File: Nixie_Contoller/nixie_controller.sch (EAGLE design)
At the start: 46 parts, among them IC1 DS1307, IC2 MAX1771ESA, IC4 MPM3630GQV-P, J1 CON-SOCJ-2155, Q1 16MHz, T1 IRF644PBF, U1 328P, U2 HU2032-LF, Y2 32.768kHz

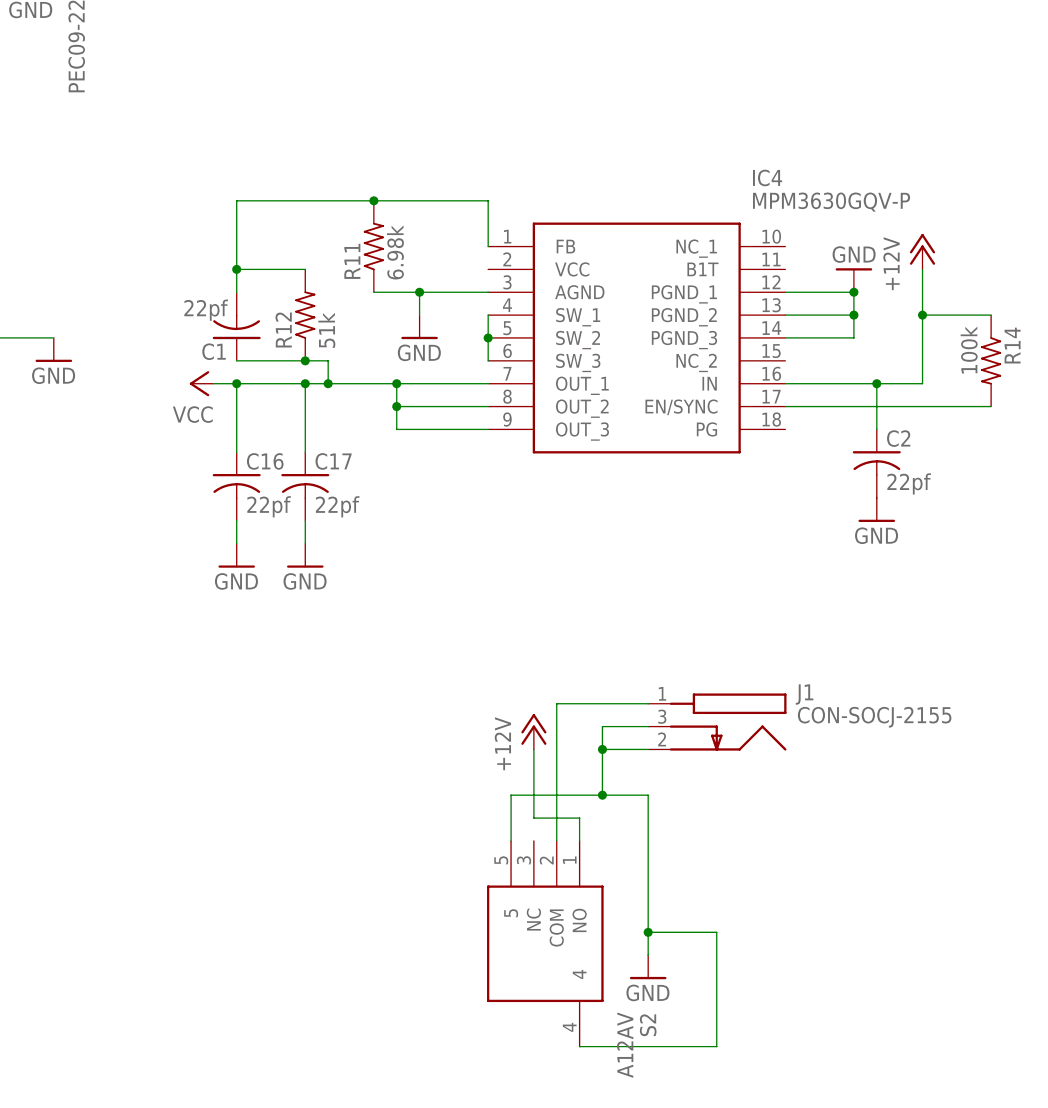
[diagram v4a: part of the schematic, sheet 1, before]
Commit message: Revert "Adds LV switching PSU"
This reverts commit 12f529c285d7cae732b9ac692bbbf0adcfd9615d.
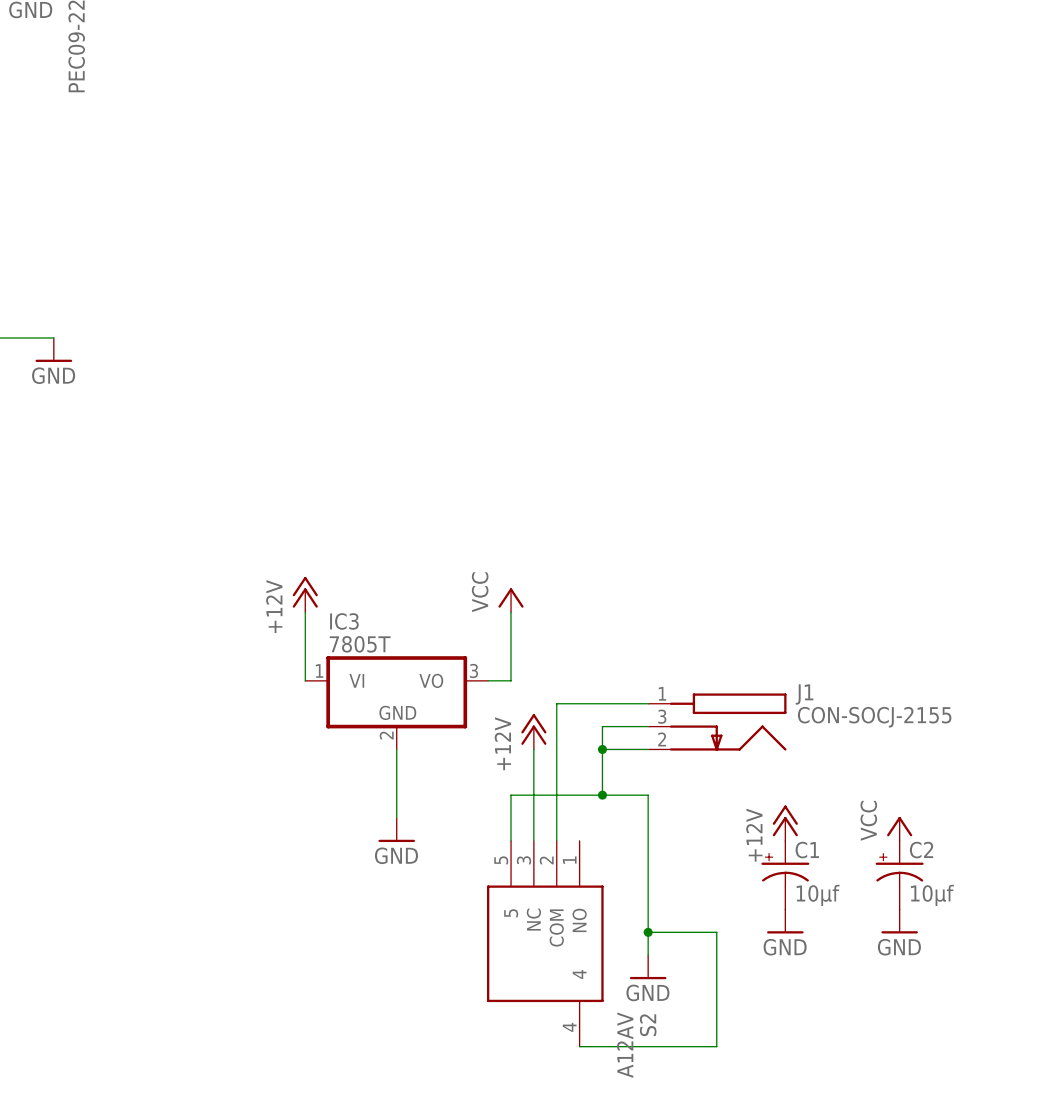
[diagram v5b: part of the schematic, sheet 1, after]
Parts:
- removed C16, C17: 22pf, rcl:C-USC0402
- removed IC4: MPM3630GQV-P, SamacSys_Parts:MPM3630GQV-P
- removed R11: 6.98k, rcl:R-US_R0201
- removed R12: 51k, rcl:R-US_R0201
- removed R14: 100k, rcl:R-US_R0201
- added IC3: 7805T, linear:7805T
- C1: value 22pf -> 10μf; device rcl:C-USC0201 -> rcl:CPOL-USE2-5
- C2: value 22pf -> 10μf; device rcl:C-USC0603 -> rcl:CPOL-USE2-5
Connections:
- removed net N$25: IC4.SW_1, IC4.SW_2, IC4.SW_3
- removed net N$28: IC4.EN/SYNC, R14.2
- removed net N$31: C1.2, IC4.FB, R11.2, R12.2
- net +12V: now also C1.+, IC3.VI, S2.NC; no longer C2.1, IC4.IN, R14.1, S2.NO
- net GND: now also C1.-, C2.-, IC3.GND; no longer C16.2, C17.2, C2.2, IC4.AGND, IC4.PGND_1, IC4.PGND_2, IC4.PGND_3, R11.1
- net VCC: now also C2.+, IC3.VO; no longer C1.1, C16.1, C17.1, IC4.OUT_1, IC4.OUT_2, IC4.OUT_3, R12.1

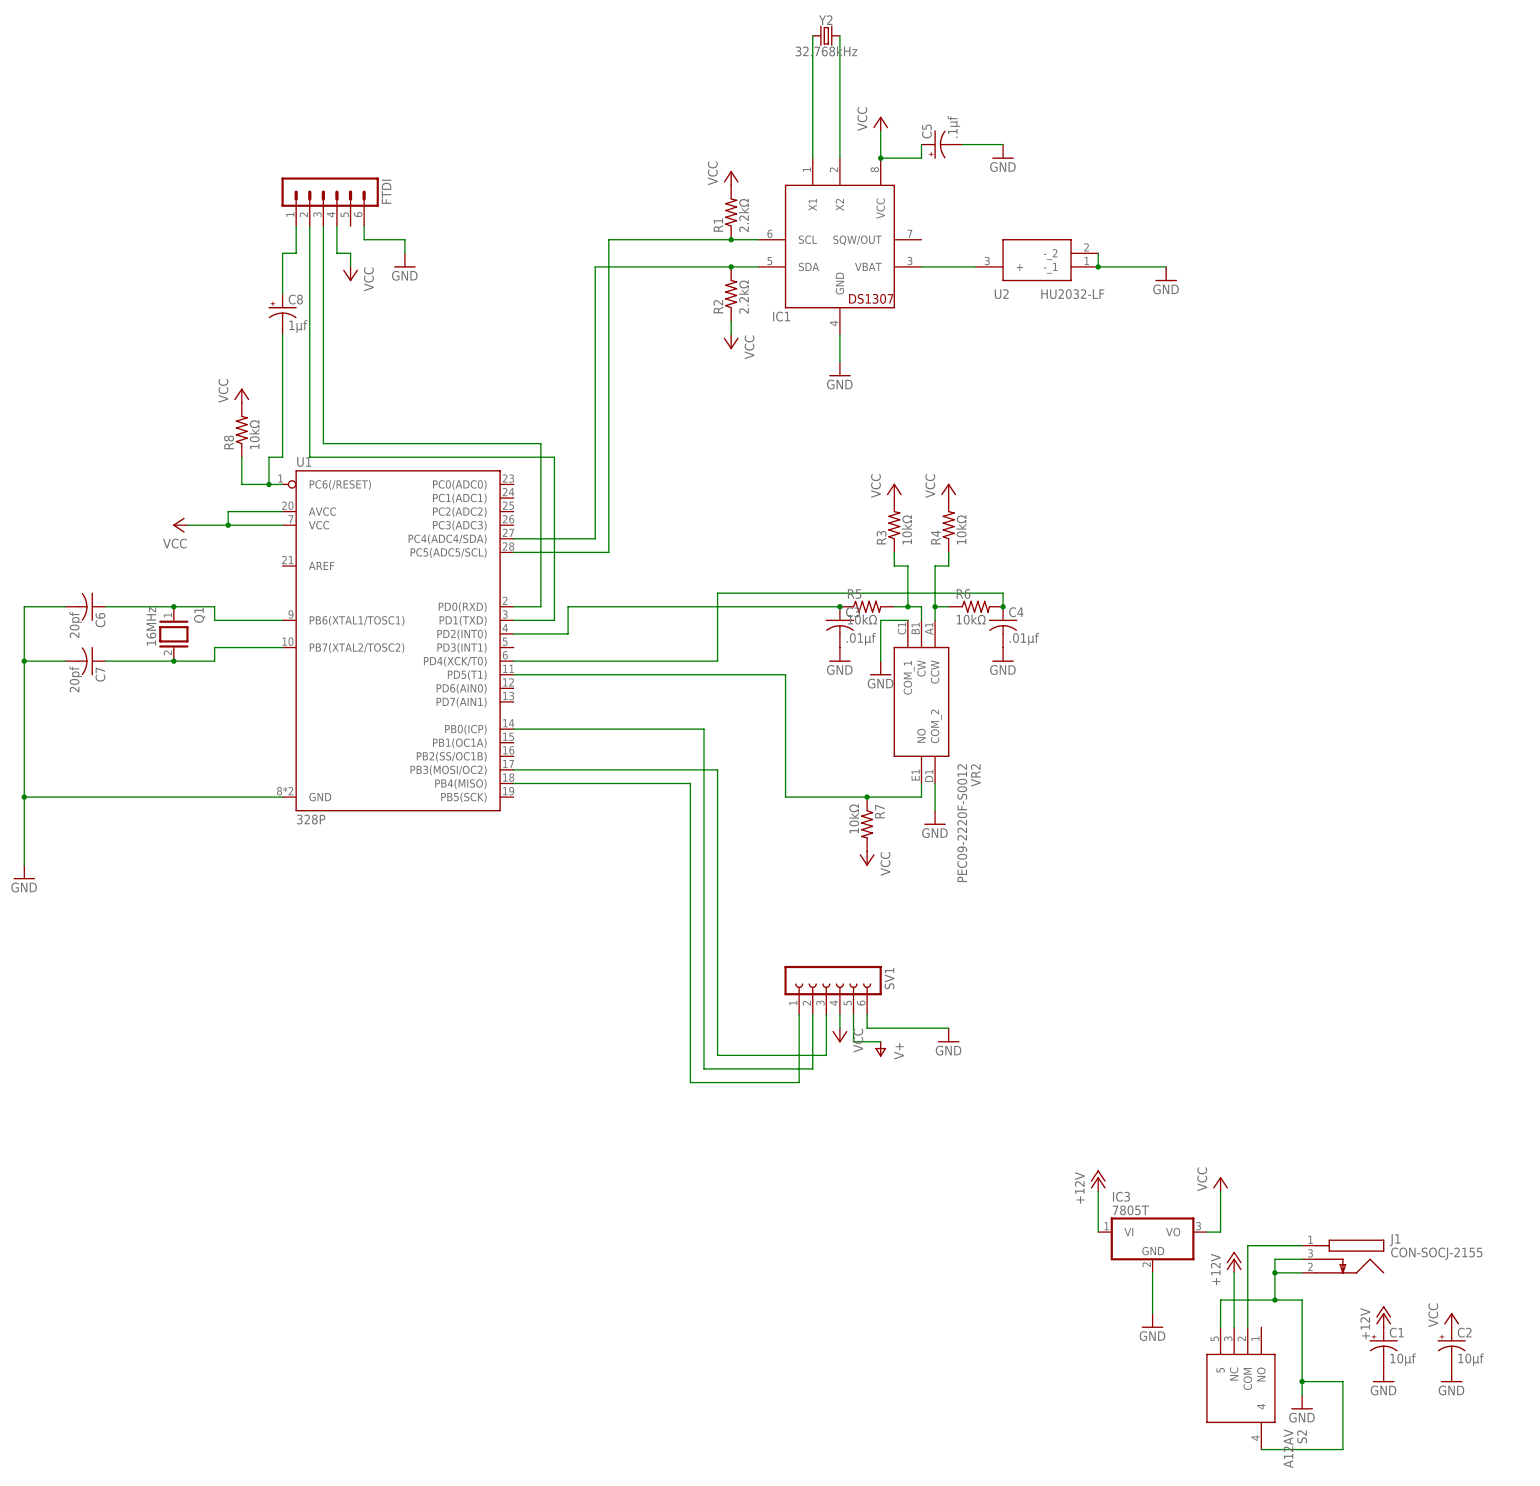
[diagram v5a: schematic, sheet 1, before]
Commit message: Shrinks board size, uses SMD components
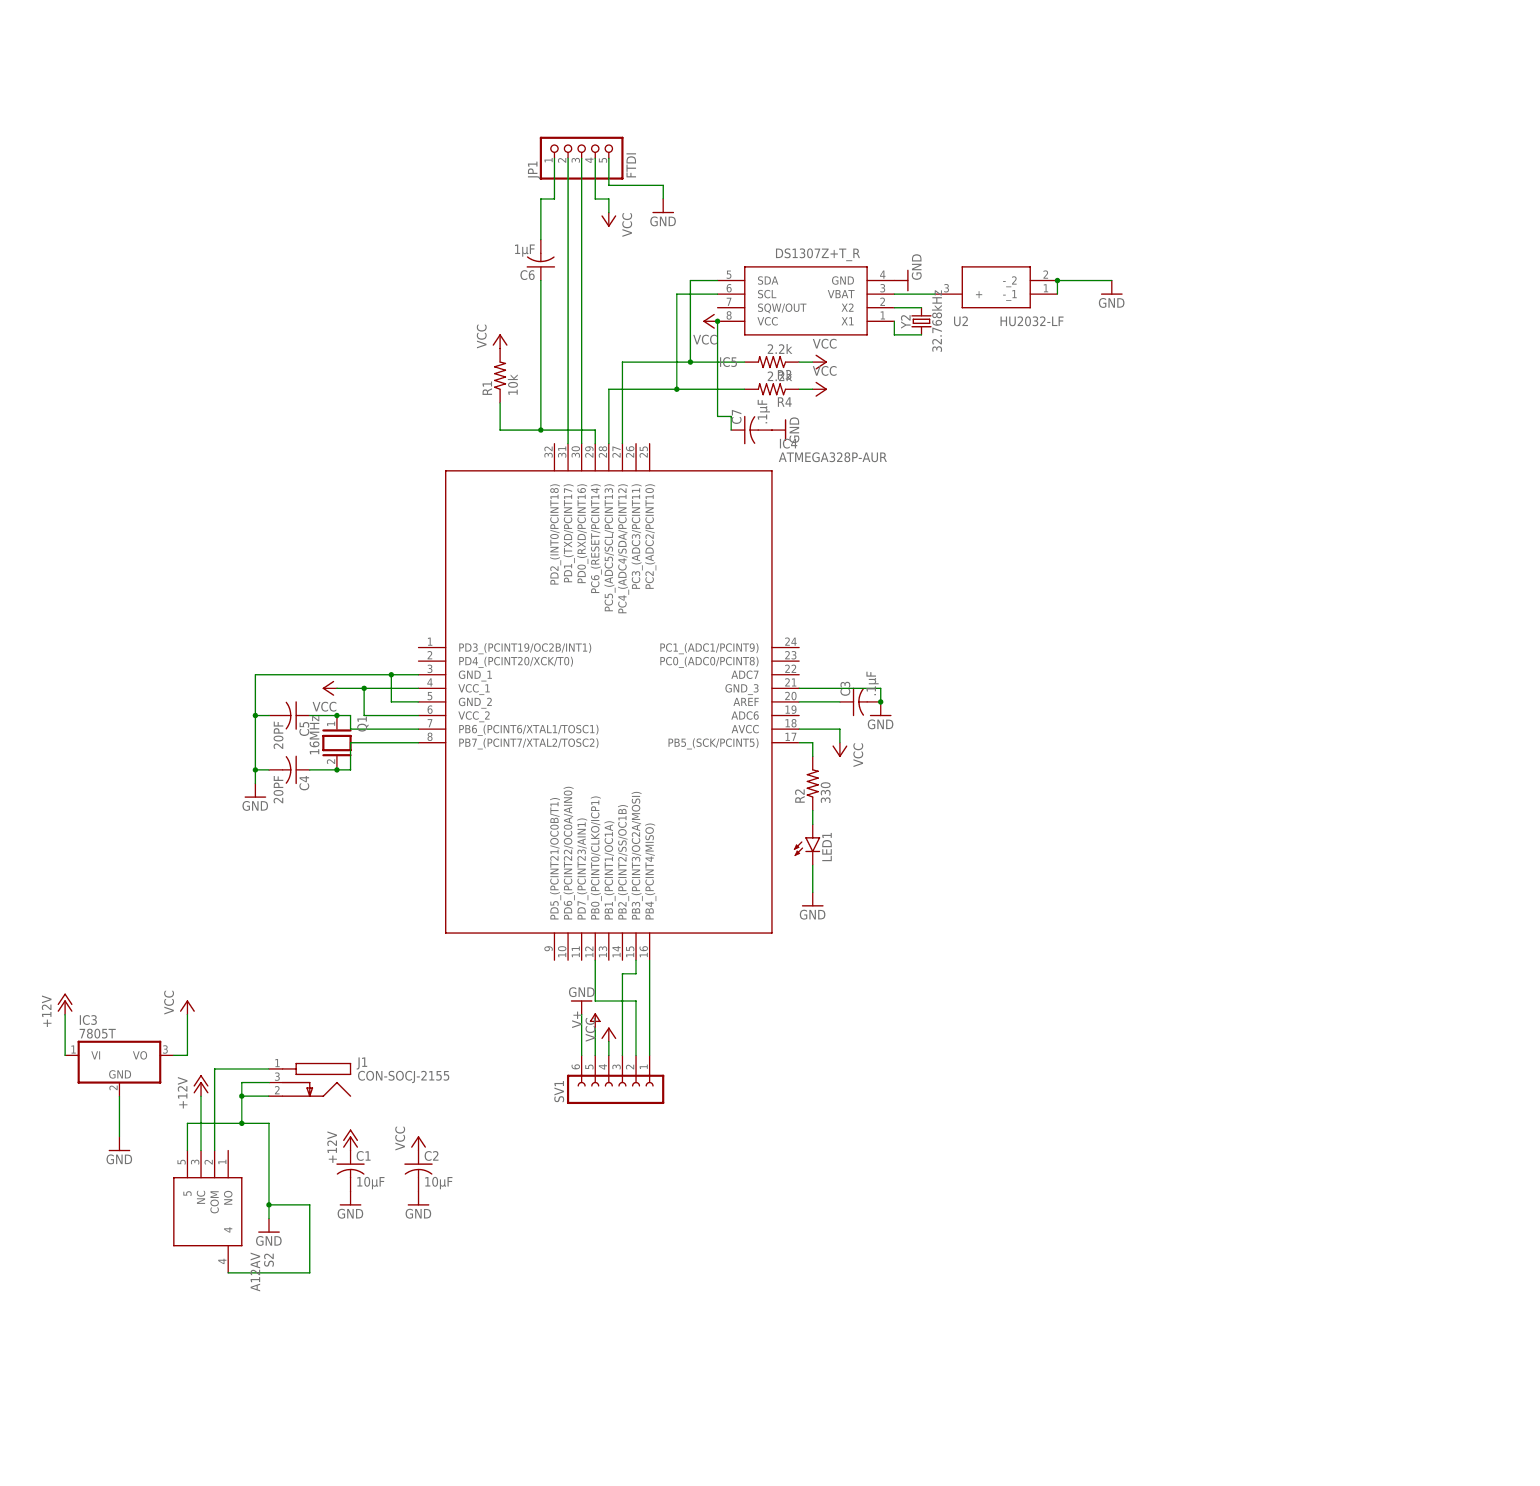
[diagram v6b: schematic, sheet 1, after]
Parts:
- removed C8: 1μf, rcl:CPOL-USE2-5
- removed FTDI: (no value), con-lstb:MA06-1
- removed IC1: DS1307, adafruit:DS1307
- removed R5, R6, R7, R8: 10kΩ, rcl:R-US_0207/10
- removed U1: 328P, SparkFun-IC-Microcontroller:ATMEGA328P_PDIP
- removed VR2: PEC09-2220F-S0012, SamacSys_Parts:PEC09-2220F-S0012
- added IC4: ATMEGA328P-AUR, SamacSys_Parts:ATMEGA328P-AUR
- added IC5: DS1307Z+T_R, SamacSys_Parts:DS1307Z+T_R
- added JP1: FTDI, pinhead:PINHD-1X5
- added LED1: (no value), led:LEDCHIP-LED0805
- C1, C2: value 10μf -> 10μF; device rcl:CPOL-USE2-5 -> rcl:C-USC0603
- C3: value .01μf -> .1μF; device rcl:C-US050-030X075 -> rcl:C-USC0603
- C4: value .01μf -> 20PF; device rcl:C-US050-030X075 -> rcl:C-USC0603
- C5: value .1μf -> 20PF; device rcl:CPOL-USE2-5 -> rcl:C-USC0603
- C6: value 20pf -> 1μF; device rcl:C-US050-030X075 -> rcl:C-USC0603
- C7: value 20pf -> .1μF; device rcl:C-US050-030X075 -> rcl:C-USC0603
- R1: value 2.2kΩ -> 10k; device rcl:R-US_0207/10 -> rcl:R-US_R0603
- R2: value 2.2kΩ -> 330; device rcl:R-US_0207/10 -> rcl:R-US_R0603
- R3, R4: value 10kΩ -> 2.2k; device rcl:R-US_0207/10 -> rcl:R-US_R0603
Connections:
- removed net N$15: R3.1, R5.2, VR2.CW
- removed net N$21: FTDI.2, U1.PD1(TXD)
- removed net N$22: FTDI.3, U1.PD0(RXD)
- new net RST: C6.1, IC4.PC6_(RESET/PCINT14), R1.1
- net +12V: now also C1.1; no longer C1.+
- net CLK: now also IC4.PB4_(PCINT4/MISO); no longer U1.PB4(MISO)
- net GND: now also C1.2, C2.2, C5.2, IC4.GND_1, IC4.GND_2, IC4.GND_3, IC5.GND, JP1.5, LED1.C; no longer C1.-, C2.-, C5.-, C6.2, FTDI.6, IC1.GND, U1.GND, VR2.COM_1, VR2.COM_2
- net N$1: now also IC5.VBAT; no longer IC1.VBAT
- net N$10: now also LED1.A, R2.1; no longer C4.1, R6.2, U1.PD4(XCK/T0)
- net N$11: now also C5.1, IC4.PB6_(PCINT6/XTAL1/TOSC1); no longer C6.1, U1.PB6(XTAL1/TOSC1)
- net N$12: now also IC4.PC4_(ADC4/SDA/PCINT12), IC5.SDA, R3.2; no longer IC1.SCL, R1.1, U1.PC5(ADC5/SCL)
- net N$13: now also IC4.PC5_(ADC5/SCL/PCINT13), IC5.SCL, R4.2; no longer IC1.SDA, R2.2, U1.PC4(ADC4/SDA)
- net N$14: now also IC4.PD0_(RXD/PCINT16), JP1.3; no longer C8.-, R8.1, U1.PC6(/RESET)
- net N$16: now also C4.1, IC4.PB7_(PCINT7/XTAL2/TOSC2); no longer C7.1, U1.PB7(XTAL2/TOSC2)
- net N$17: now also C6.2, JP1.1; no longer C8.+, FTDI.1
- net N$18: now also IC4.PB3_(PCINT3/OC2A/MOSI); no longer U1.PB3(MOSI/OC2)
- net N$2: now also IC4.PD1_(TXD/PCINT17), JP1.2; no longer R7.1, U1.PD5(T1), VR2.NO
- net N$3: now also IC4.PB5_(SCK/PCINT5), R2.2; no longer R4.1, R6.1, VR2.CCW
- net N$4: now also IC5.X2, Y2.2; no longer IC1.X1, Y2.1
- net N$5: now also IC5.X1, Y2.1; no longer IC1.X2, Y2.2
- net N$7: now also IC4.PB0_(PCINT0/CLKO/ICP1); no longer U1.PB0(ICP)
- net N$9: now also IC4.AREF; no longer R5.1, U1.PD2(INT0)
- net VCC: now also C2.1, C7.1, IC4.AVCC, IC4.VCC_1, IC4.VCC_2, IC5.VCC, JP1.4, R3.1, R4.1; no longer C2.+, C5.+, FTDI.4, IC1.VCC, R2.1, R3.2, R4.2, R7.2, R8.2, U1.AVCC, U1.VCC
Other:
- moved on the sheet: C3, C4, C6, C7, IC3, J1, Q1, R1, R2, R3, R4, S2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
